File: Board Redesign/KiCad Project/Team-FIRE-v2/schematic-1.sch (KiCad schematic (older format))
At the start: 32 parts, among them J1 SIM_Card, J2 53885-0408, U1 TPS40210DGQR, U2 NCN4555MN, U3 CSD18543Q3A

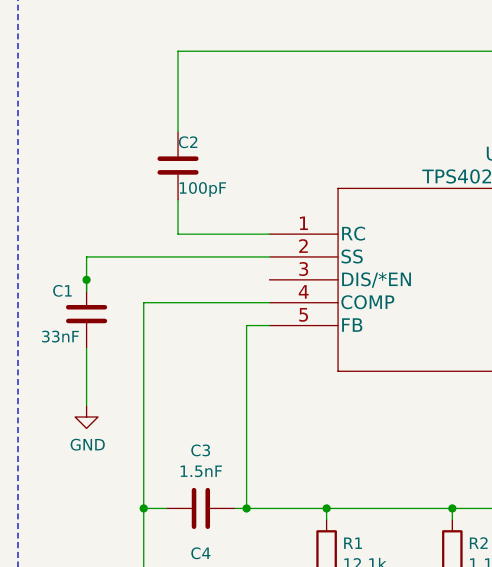
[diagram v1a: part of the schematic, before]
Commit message: Starting complete BOM generation
- Finished schematic(s)
- Started BOM information assignment for final BOM sent to NASA
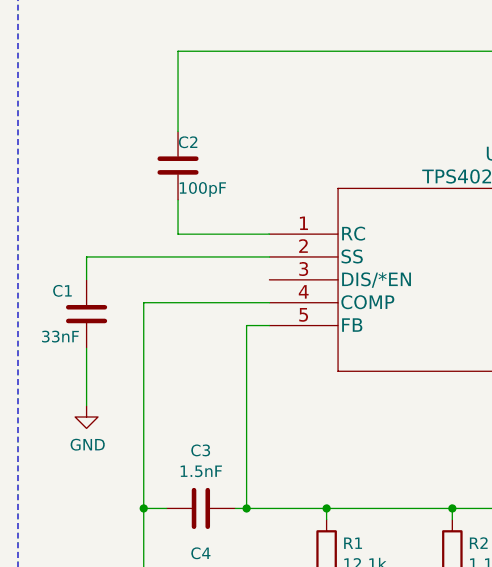
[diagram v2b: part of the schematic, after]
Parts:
- C1: Link (none) -> https://www.mouser.com/ProductDetail/KEMET/C0603C333J1RECTU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; MPN (none) -> C0603C333J1RECTU; Manufacturer (none) -> KEMET; Supplier (none) -> Mouser; Supplier PN (none) -> 80-C0603C333J1REC; Tolerance (none) -> 5%; Type (none) -> Ceramic X7R Capacitor; Voltage Rating (none) -> 100 VDC
- C2: Link (none) -> https://www.mouser.com/ProductDetail/KEMET/CBR06C101F5GAC?q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; MPN (none) -> CBR06C101F5GAC; Manufacturer (none) -> KEMET; Supplier PN (none) -> 80-CBR06C101F5GAC; Tolerance (none) -> 1%; Type (none) -> Ceramic C0G Capacitor; Voltage Rating (none) -> 50 VDC
- R3: footprint (none) -> Resistor_SMD:R_0603_1608Metric; Link (none) -> https://www.mouser.com/ProductDetail/Vishay-Dale/CRCW060330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; MPN (none) -> CRCW0603301KFKEAHP; Manufacturer (none) -> Vishay; Qualification (none) -> AEC-Q200; Supplier (none) -> Mouser; Tolerance (none) -> 1%; Type (none) -> Thick Film Resistors; Voltage Rating (none) -> 75 V
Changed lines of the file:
@@
 EESchema Schematic File Version 4
+LIBS:Team-FIRE-v2-cache
 EELAYER 30 0
 EELAYER END
@@
 F 2 "Capacitor_SMD:C_0603_1608Metric" H 1488 1800 50  0001 C CNN
 F 3 "~" H 1450 1950 50  0001 C CNN
+F 4 "CBR06C101F5GAC" H 1450 1950 50  0001 C CNN "MPN"
+F 5 "KEMET" H 1450 1950 50  0001 C CNN "Manufacturer"
+F 6 "https://www.mouser.com/ProductDetail/KEMET/CBR06C101F5GAC?qs=sGAEpiMZZMs0AnBnWHyRQN7%2FAA2D2lPPUdZo0nHgvrj7UthX3WhjQw%3D%3D" H 1450 1950 50  0001 C CNN "Link"
+F 7 "80-CBR06C101F5GAC" H 1450 1950 50  0001 C CNN "Supplier PN"
+F 8 "Ceramic C0G Capacitor" H 1450 1950 50  0001 C CNN "Type"
+F 9 "1%" H 1450 1950 50  0001 C CNN "Tolerance"
+F 10 "50 VDC" H 1450 1950 50  0001 C CNN "Voltage Rating"
 	1    1450 1950
 	1    0    0    -1
@@
 F 1 "33nF" H 850 2500 50  0000 L CNN
 F 2 "Capacitor_SMD:C_0603_1608Metric" H 1088 2450 50  0001 C CNN
-F 3 "~" H 1050 2600 50  0001 C CNN
+F 3 "https://www.mouser.com/datasheet/2/212/KEM_C1090_X7R_ESD-1103328.pdf" H 1050 2600 50  0001 C CNN
+F 4 "C0603C333J1RECTU" H 1050 2600 50  0001 C CNN "MPN"
+F 5 "KEMET" H 1050 2600 50  0001 C CNN "Manufacturer"
+F 6 "https://www.mouser.com/ProductDetail/KEMET/C0603C333J1RECTU?qs=%2Fha2pyFaduhO0BMCJt7%2F4e6aB%252BbzjNiI6sPRWR3SWdVo%252BW61sHPT%252BQ%3D%3D" H 1050 2600 50  0001 C CNN "Link"
+F 7 "80-C0603C333J1REC" H 1050 2600 50  0001 C CNN "Supplier PN"
+F 8 "Mouser" H 1050 2600 50  0001 C CNN "Supplier"
+F 9 "Ceramic X7R Capacitor" H 1050 2600 50  0001 C CNN "Type"
+F 10 "5%" H 1050 2600 50  0001 C CNN "Tolerance"
+F 11 "100 VDC" H 1050 2600 50  0001 C CNN "Voltage Rating"
 	1    1050 2600
 	1    0    0    -1
@@
 F 0 "R3" V 3150 1400 50  0000 L CNN
 F 1 "301k" V 2950 1350 50  0000 L CNN
-F 2 "" V 2980 1450 50  0001 C CNN
-F 3 "~" H 3050 1450 50  0001 C CNN
+F 2 "Resistor_SMD:R_0603_1608Metric" V 2980 1450 50  0001 C CNN
+F 3 "https://www.mouser.com/datasheet/2/427/crcwhpe3-1713858.pdf" H 3050 1450 50  0001 C CNN
+F 4 "CRCW0603301KFKEAHP" V 3050 1450 50  0001 C CNN "MPN"
+F 5 "Thick Film Resistors" V 3050 1450 50  0001 C CNN "Type"
+F 6 "75 V" V 3050 1450 50  0001 C CNN "Voltage Rating"
+F 7 "Vishay" V 3050 1450 50  0001 C CNN "Manufacturer"
+F 8 "Mouser" V 3050 1450 50  0001 C CNN "Supplier"
+F 9 "https://www.mouser.com/ProductDetail/Vishay-Dale/CRCW0603301KFKEAHP?qs=sGAEpiMZZMtlubZbdhIBILDMOtf4qnQoMDmfFrlZC70%3D" V 3050 1450 50  0001 C CNN "Link"
+F 10 "1%" V 3050 1450 50  0001 C CNN "Tolerance"
+F 11 "AEC-Q200" V 3050 1450 50  0001 C CNN "Qualification"
 	1    3050 1450
 	0    -1   -1   0
@@
 	1300 3450 1300 3900
 Wire Wire Line
-	1050 2500 1050 2450
-Wire Wire Line
 	1050 2350 1850 2350
-Connection ~ 1050 2450
 Wire Wire Line
 	1050 2450 1050 2350
@@
 	6850 800  6850 4800
 $Comp
-L power:+5V #PWR?
+L power:+5V #PWR0125
 U 1 1 5EA85382
 P 7450 3000
-F 0 "#PWR?" H 7450 2850 50  0001 C CNN
+F 0 "#PWR0125" H 7450 2850 50  0001 C CNN
 F 1 "+5V" V 7465 3128 50  0000 L CNN
 F 2 "" H 7450 3000 50  0001 C CNN
@@
 $EndComp
 $Comp
-L power:+5V #PWR?
+L power:+5V #PWR0126
 U 1 1 5EA858F2
 P 1950 6000
-F 0 "#PWR?" H 1950 5850 50  0001 C CNN
+F 0 "#PWR0126" H 1950 5850 50  0001 C CNN
 F 1 "+5V" V 1965 6128 50  0000 L CNN
 F 2 "" H 1950 6000 50  0001 C CNN

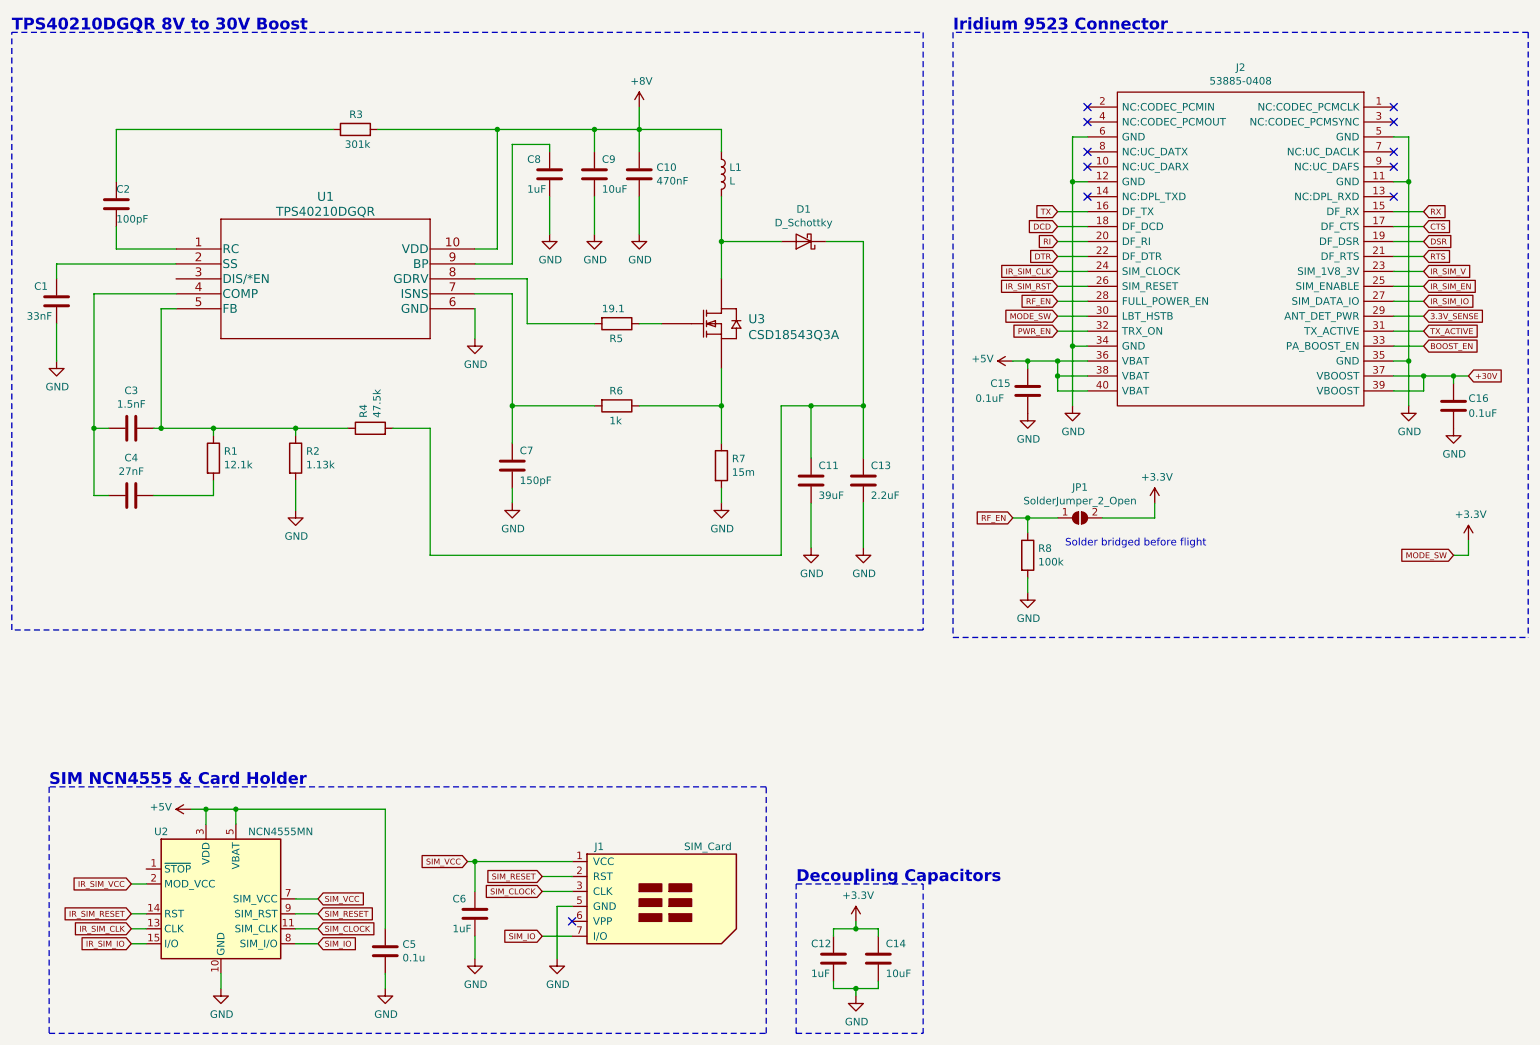
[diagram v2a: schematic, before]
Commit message: Fixed libraries, added BOM info to most components
- Fixed MCP1826T library to be a part of Team-Fire library (not separate)
- Deleted useless library files for various pieces (such as ImportGuides, etc.)
- Fixed inductor value specification for boost converter
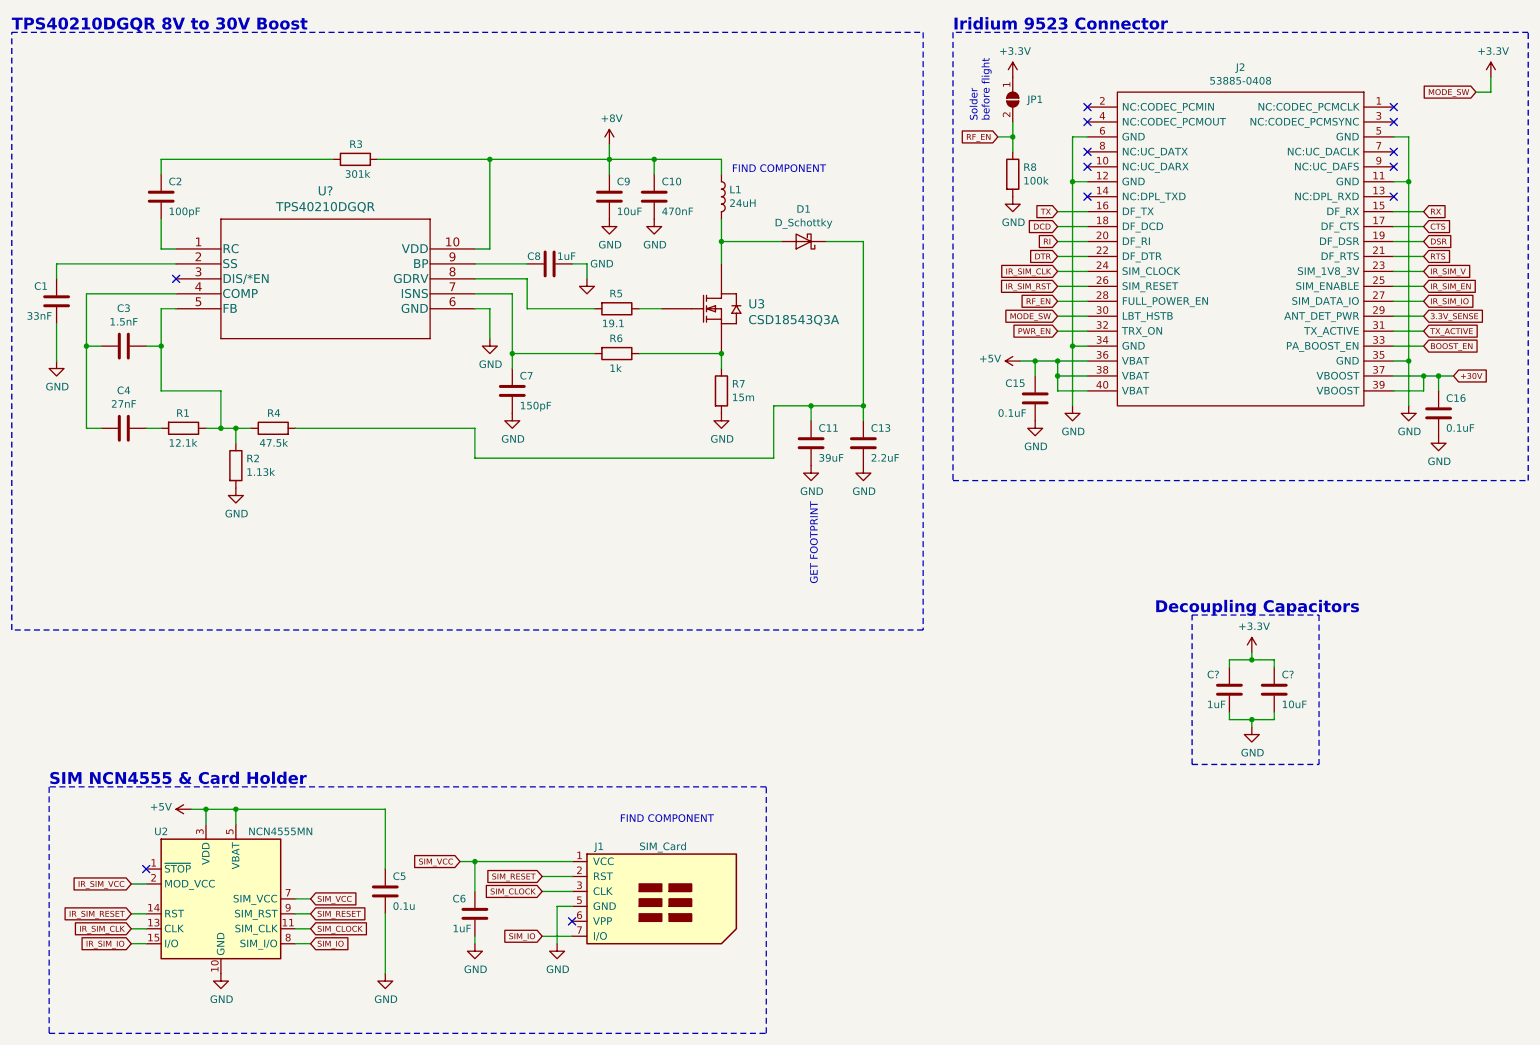
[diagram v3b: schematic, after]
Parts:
- removed C12: 1uF, Capacitor_SMD:C_0603_1608Metric, symbol Device:C
- removed C14: 10uF, Capacitor_SMD:C_0603_1608Metric, symbol Device:C
- removed U1: TPS40210DGQR, DGQ10_1P88X1P57, symbol Boost_chip_v3:TPS40210DGQR
- added C?: 1uF, Capacitor_SMD:C_0603_1608Metric, symbol Device:C
- added C?: 10uF, Capacitor_SMD:C_0603_1608Metric, symbol Device:C
- added U?: TPS40210DGQR, Team-FIRE:TPS40210DGQR, symbol Team-FIRE:TPS40210DGQR
- C10: Link (none) -> https://www.mouser.com/ProductDetail/KEMET/C0603C474J4RACAU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; MPN (none) -> C0603C474J4RACAUTO; Manufacturer (none) -> KEMET; Qualification (none) -> AEC-Q200; Supplier (none) -> Mouser; Supplier PN (none) -> 80-C0603C474J4RAUTO; Tolerance (none) -> 5%; Type (none) -> Ceramic X7R; Voltage Rating (none) -> 16 VDC
- C11: footprint Capacitor_SMD:C_0603_1608Metric -> (none); Link (none) -> https://www.mouser.com/ProductDetail/Panasonic/EEE-FK1H390S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; MPN (none) -> EEE-FK1H390SV; Manufacturer (none) -> Panasonic; Qualification (none) -> AEC-Q200; Supplier (none) -> Mouser; Supplier PN (none) -> 667-EEE-FK1H390SV; Tolerance (none) -> 20%; Type (none) -> Aluminum Electrolytic Capacitors; Voltage Rating (none) -> 50 VDC
- C15, C16, C5: Link (none) -> https://www.mouser.com/ProductDetail/KEMET/C0603C104K5RAC31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; MPN (none) -> C0603C104K5RAC3121; Manufacturer (none) -> KEMET; Qualification (none) -> AEC-Q200; Supplier (none) -> Mouser; Supplier PN (none) -> 80-C603C104K5RAC3121; Tolerance (none) -> 10%; Type (none) -> Ceramic X7R Capacitor; Voltage Rating (none) -> 50 VDC
- C3: footprint (none) -> Capacitor_SMD:C_0603_1608Metric; Link (none) -> https://www.mouser.com/ProductDetail/TDK/C1608C0G2A152J080A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; MPN (none) -> C1608C0G2A152J080AE; Manufacturer (none) -> TDK; Supplier (none) -> Mouser; Supplier PN (none) -> 810-C1608C0G2A152J08; Tolerance (none) -> 5%; Type (none) -> Ceramic C0G Capacitor; Voltage Rating (none) -> 100 VDC
- C4: footprint (none) -> Capacitor_SMD:C_0603_1608Metric; Link (none) -> https://www.mouser.com/ProductDetail/KEMET/C0603C273J3RACTU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; MPN (none) -> C0603C273J3RACTU; Manufacturer (none) -> KEMET; Supplier (none) -> Mouser; Supplier PN (none) -> 80-C0603C273J3R; Tolerance (none) -> 5%; Type (none) -> Ceramic X7R Capacitor; Voltage Rating (none) -> 25 VDC
- C6: Link (none) -> https://www.mouser.com/ProductDetail/Taiyo-Yuden/TMK107BLD1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; MPN (none) -> TMK107BLD105KA-T; Manufacturer (none) -> Taiyo Yuden; Supplier (none) -> Mouser; Supplier PN (none) -> 963-TMK107BLD105KA-T; Tolerance (none) -> 10%; Type (none) -> Ceramic X5R Capacitor; Voltage Rating (none) -> 25 VDC
- C9: Link (none) -> https://www.mouser.com/ProductDetail/Murata-Electronics/GRM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; MPN (none) -> GRM188R61E106KA73D; Manufacturer (none) -> Murata; Supplier (none) -> Mouser; Supplier PN (none) -> 81-GRM188R61E106KA73D; Tolerance (none) -> 10%; Type (none) -> Ceramic X5R Capacitor; Voltage Rating (none) -> 25 VDC
- L1: value L -> 24uH
- R1: footprint (none) -> Resistor_SMD:R_0603_1608Metric; Link (none) -> https://www.mouser.com/ProductDetail/Panasonic/ERJ-PB3B1212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; MPN (none) -> ERJ-PB3B1212V; Manufacturer (none) -> Panasonic; Qualification (none) -> AEC-Q200; Supplier (none) -> Mouser; Supplier PN (none) -> 667-ERJ-PB3B1212V; Tolerance (none) -> 0.1%; Type (none) -> Thick Film Resistors
- R2: footprint (none) -> Resistor_SMD:R_0603_1608Metric; Link (none) -> https://www.mouser.com/ProductDetail/TE-Connectivity-Holswo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; MPN (none) -> RQ73C1J1K13BTDF; Manufacturer (none) -> TE Connectivity; Qualification (none) -> AEC-Q200; Supplier (none) -> Mouser; Supplier PN (none) -> 279-RQ73C1J1K13BTDF; Tolerance (none) -> 0.1%; Type (none) -> Thin Film Resistor
- R4: footprint (none) -> Resistor_SMD:R_0603_1608Metric; Link (none) -> https://www.mouser.com/ProductDetail/Vishay-Beyschlag/MCT06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; MPN (none) -> MCT06030C4752FP500; Manufacturer (none) -> Vishay; Supplier (none) -> Mouser; Supplier PN (none) -> 594-MCT06030C4752FP5; Tolerance (none) -> 1%; Type (none) -> Thin Film Resistors; Voltage Rating (none) -> 75 V
- R5: footprint (none) -> Resistor_SMD:R_0603_1608Metric; Link (none) -> https://www.mouser.com/ProductDetail/Panasonic/ERJ-3EKF19R1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; MPN (none) -> ERJ-3EKF19R1V; Manufacturer (none) -> Panasonic; Qualification (none) -> AEC-Q200; Supplier (none) -> Mouser; Supplier PN (none) -> 667-ERJ-3EKF19R1V; Tolerance (none) -> 1%; Type (none) -> Thick Film Resistors; Voltage Rating (none) -> 75 V
- R6: Link (none) -> https://www.mouser.com/ProductDetail/Vishay-Beyschlag/MCT06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; MPN (none) -> MCT0603MD1001BP500; Manufacturer (none) -> Vishay; Supplier (none) -> Mouser; Supplier PN (none) -> 594-MCT0603MD1001BP5; Tolerance (none) -> 0.1%; Type (none) -> Thin Film Resistor; Voltage Rating (none) -> 75 V
- R7: footprint (none) -> Resistor_SMD:R_0603_1608Metric; Link (none) -> https://www.mouser.com/ProductDetail/ARCOL-Ohmite/LVT06R015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; MPN (none) -> LVT06R0150FER; Manufacturer (none) -> Ohmite; Supplier (none) -> Mouser; Supplier PN (none) -> 588-LVT06R0150FER; Tolerance (none) -> 1%; Type (none) -> Current Sense Resistors
- R8: Link (none) -> https://www.mouser.com/ProductDetail/Vishay-Beyschlag/MCT06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; MPN (none) -> MCT06030E1003BP500; Manufacturer (none) -> Vishay; Supplier (none) -> Mouser; Supplier PN (none) -> 594-MCT06030E1003BP5; Tolerance (none) -> 0.1%; Type (none) -> Thin Film Resistors; Voltage Rating (none) -> 75 V
- U2: Description (none) -> Voltage level shifter; Link (none) -> https://www.mouser.com/ProductDetail/ON-Semiconductor/NCN45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; Manufacturer (none) -> ON Semiconductor; Supplier (none) -> Mouser; Supplier PN (none) -> 863-NCN4555MNR2G
- U3: footprint DNH0008A -> Package_SON:VSON-8_3.3x3.3mm_P0.65mm_NexFET; Description (none) -> Boost MOSFET; Link (none) -> https://www.mouser.com/ProductDetail/Texas-Instruments/CSD1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; MPN (none) -> CSD18543Q3A; Manufacturer (none) -> Texas Instruments; Supplier (none) -> Mouser; Supplier PN (none) -> 595-CSD18543Q3A; Type (none) -> MOSFET
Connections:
- net +3V3: now also JP1.1 (A), C?.1, C?.1; no longer JP1.2 (B)
- net +8V: now also U?.10 (VDD)
- net GND: now also C8.1, C?.2, C?.2, U?.6 (GND); no longer C8.2
- net RF_EN: now also JP1.2 (B); no longer JP1.1 (A)
- net at C3.2, C4.2: now also U?.4 (COMP)
- net at C3.1, R1.1, R2.1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: now also U?.5 (FB)
- net at C2.2: now also U?.1 (RC)
- net at C1.1: now also U?.2 (SS)
- net at R5.2: now also U?.8 (GDRV)
- net at C7.1, R6.2: now also U?.7 (ISNS)
- new net: C8.2, U?.9 (BP)
- no-connect marks 11 -> 13
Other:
- note added: "FIND COMPONENT"
- note added: "GET FOOTPRINT"
- note added: "Solder\nbefore flight"
- note removed: "Solder bridged before flight"
- moved on the sheet: C10, C11, C13, C15, C2, C3, C4, C5, C7, C8, C9, JP1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
